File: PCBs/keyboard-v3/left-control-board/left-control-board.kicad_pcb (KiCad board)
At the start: 2 copper layers, 110.9 x 40 mm, 51 parts, among them J101 USB4510-03-1-A, J102 USB4510-03-1-A, J103 AMPHENOL_GSB12J21C1EU, J105 MSD-1-A, J501 Conn_02x08_Odd_Even, J601 F31Z1A7H111008, J602 F31Z1A7H111008, U101 USB2534-1080AEN, U102 STM32G0C1CEUx, U103 GL835, U104 USBLC6-4SC6, U201 USBLC6-4SC6, U701 TPS62290TDRVRQ1, Y101 CX2016SA24000D0HLLG3

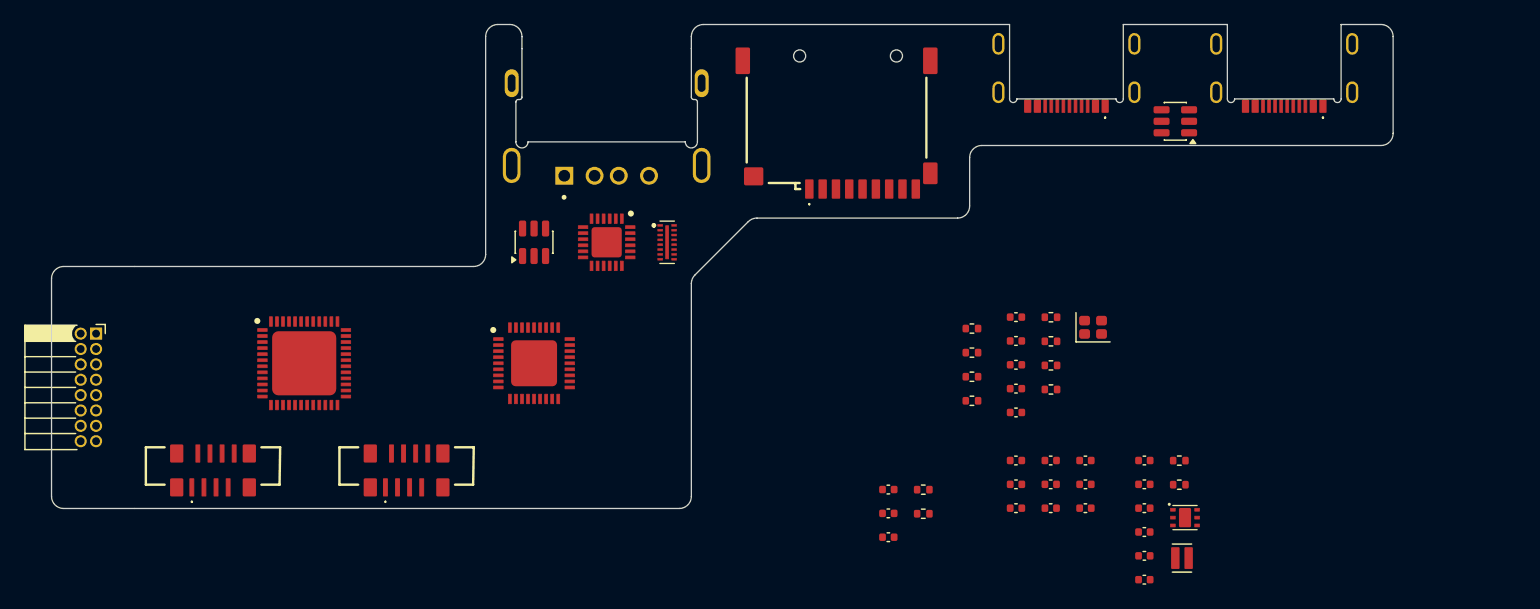
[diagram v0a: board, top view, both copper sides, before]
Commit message: Left knob board done
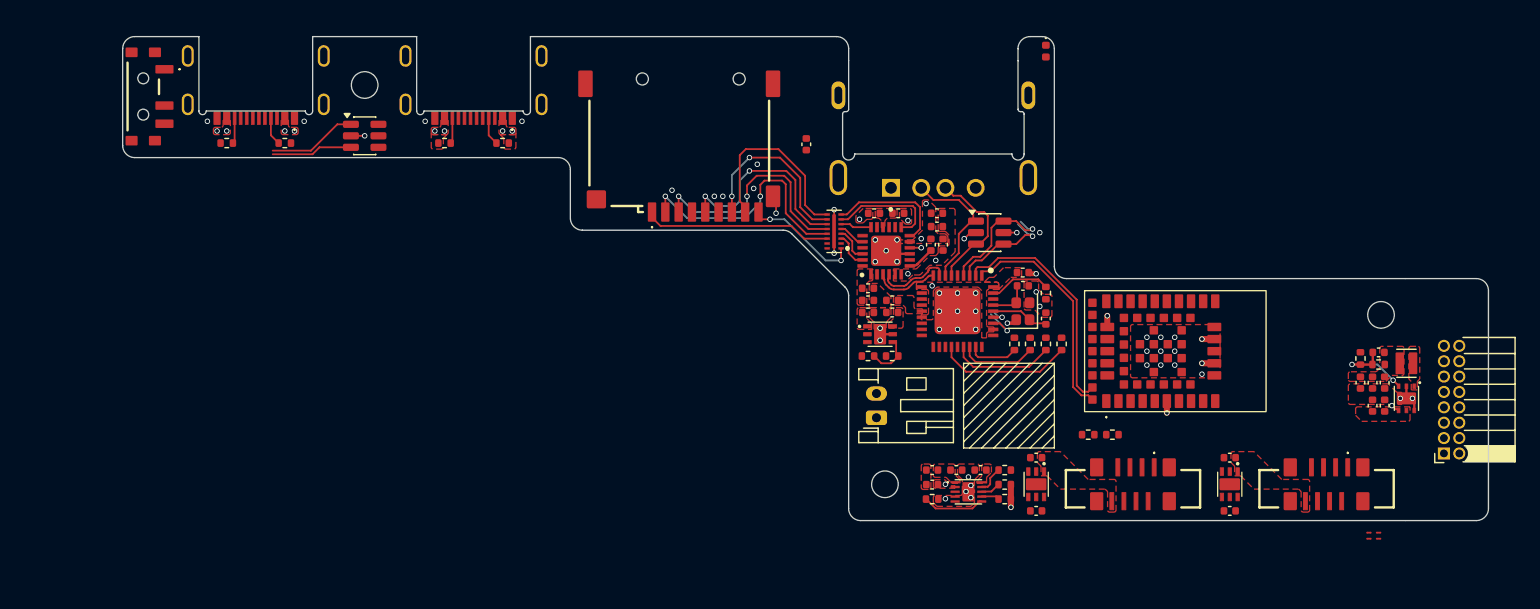
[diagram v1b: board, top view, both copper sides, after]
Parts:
- removed C109: 100n, project_footprints:C_0402
- removed C110: 1u, project_footprints:C_0402
- removed C111, C201, C202, C204, C205, C206: 4u7, project_footprints:C_0402
- removed C203: 22p, project_footprints:C_0402
- removed L201: 78438313015, project_footprints:L_Wurth_WE-MAIA-1610
- removed R101, R102: 10k, project_footprints:R_0402
- removed R203, R204: 5k1, project_footprints:R_0402
- removed U102: STM32G0C1CEUx, project_footprints:QFN50P700X700X60-49N-D
- added C601: 1u, project_footprints:C_0402, F.Cu at (175.5, 118.2)
- added C602: 1u, project_footprints:C_0402, F.Cu at (175.5, 113.8)
- added C603: 1u, project_footprints:C_0402, F.Cu at (191.5, 118.2)
- added C604: 1u, project_footprints:C_0402, F.Cu at (191.5, 113.8)
- added C701: 1u, project_footprints:C_0402, F.Cu at (170.9, 114.8)
- added C702: 4u7, project_footprints:C_0402, F.Cu at (168.9, 114.8)
- added C703: 4u7, project_footprints:C_0402, F.Cu at (166.9, 114.8)
- added C704: 1u, project_footprints:C_0402, F.Cu at (166.9, 116.0)
- added C705: 4u7, project_footprints:C_0402, F.Cu at (204.3, 109.5)
- added C706: 4u7, project_footprints:C_0402, F.Cu at (203.3, 109.5)
- added C707: 22p, project_footprints:C_0402, F.Cu at (203.8, 105.1)
- added C708: 4u7, project_footprints:C_0402, F.Cu at (204.3, 107.6)
- added C709: 4u7, project_footprints:C_0402, F.Cu at (203.3, 107.6)
- added C710: 4u7, project_footprints:C_0402, F.Cu at (202.3, 107.6)
- added C803: 1u, project_footprints:C_0402, F.Cu at (163.6, 101.8)
- added D701: RED, project_footprints:LED_0402, F.Cu at (176.3, 80.2)
- added H101: MountingHole, MountingHole:MountingHole_2.2mm_M2, F.Cu at (120.0, 83.0)
- added H102: MountingHole, MountingHole:MountingHole_2.2mm_M2, F.Cu at (163.0, 116.0)
- added H103: MountingHole, MountingHole:MountingHole_2.2mm_M2, F.Cu at (204.0, 102.0)
- added J701: Conn_01x02, Connector_JST:JST_PH_S2B-PH-K_1x02_P2.00mm_Horizontal, F.Cu at (162.3, 110.5)
- added L701: 78438313015, project_footprints:L_Wurth_WE-MAIA-1610, F.Cu at (206.1, 106.0)
- added NT601: NetTie_2, project_footprints:NetTie-2_SMD_Pad0.15mm, F.Cu at (203.0, 120.5)
- added NT602: NetTie_2, project_footprints:NetTie-2_SMD_Pad0.15mm, F.Cu at (203.0, 120.0)
- added NT603: NetTie_2, project_footprints:NetTie-2_SMD_Pad0.15mm, F.Cu at (203.8, 120.5)
- added NT604: NetTie_2, project_footprints:NetTie-2_SMD_Pad0.15mm, F.Cu at (203.8, 120.0)
- added R205: 5k1, project_footprints:R_0402, F.Cu at (108.6, 87.8)
- added R206: 5k1, project_footprints:R_0402, F.Cu at (113.4, 87.8)
- added R401: 806k, project_footprints:R_0402, F.Cu at (179.8, 111.9)
- added R402: 2M, project_footprints:R_0402, F.Cu at (181.8, 111.9)
- added R703: 13k, project_footprints:R_0402, F.Cu at (172.9, 117.2)
- added R704: 10k, project_footprints:R_0402, F.Cu at (166.9, 117.2)
- added R705: 806k, project_footprints:R_0402, F.Cu at (203.8, 106.1)
- added R706: 180k, project_footprints:R_0402, F.Cu at (202.3, 105.6)
- added R803: 10k, project_footprints:R_0402, F.Cu at (177.6, 104.4)
- added R804: 10k, project_footprints:R_0402, F.Cu at (176.3, 104.4)
- added R807: 10k, project_footprints:R_0402, F.Cu at (173.7, 104.4)
- added S701: PCM12SMTBR, project_footprints:PCM12SMTBR, F.Cu at (101.7, 84.0)
- added U401: NINA-B302-00B, project_footprints:NINAB30200B, F.Cu at (187.0, 105.0)
- added U601: NCP380HMU05AATBG, project_footprints:SON65P200X200X55-7N, F.Cu at (175.5, 116.0)
- added U602: NCP380HMU05AATBG, project_footprints:SON65P200X200X55-7N, F.Cu at (191.5, 116.0)
- added U702: TPS62290TDRVRQ1, project_footprints:SON65P200X200X80-7N, F.Cu at (206.1, 108.9)
- added U801: NCP380HMU05AATBG, project_footprints:SON65P200X200X55-7N, F.Cu at (162.6, 103.6)
- J204: renamed from J103; value AMPHENOL_GSB12J21C1EU -> GSB12J21C1EU
- R201, R202: value 5k1 -> 22k
- R701: value 820k -> 10k
- R702: value 182k -> 1k
- U701: value TPS62290TDRVRQ1 -> BQ25185DLHR; footprint project_footprints:SON65P200X200X80-7N -> project_footprints:SON40P220X200X80-11N
- moved J501 111.8 mm to (209.2, 113.5), turned to 180 degrees
- moved J602 92.0 mm to (199.5, 116.0), turned to 0 degrees
- moved J201 85.0 mm to (111.0, 79.0)
- moved J601 60.1 mm to (183.5, 116.0), turned to 0 degrees
- moved J202 49.0 mm to (129.0, 79.0)
- moved R202 46.9 mm to (126.6, 87.8)
- moved R201 41.7 mm to (131.4, 87.8), turned to 180 degrees
- moved C308 36.4 mm to (156.5, 87.9), turned to -90 degrees
- moved U802 35.3 mm to (169.0, 101.7), turned to -90 degrees
- moved J204 27.0 mm to (167.0, 81.0)
- moved C302 25.3 mm to (162.1, 93.6), turned to 180 degrees
- moved C309 25.2 mm to (166.8, 96.2), turned to 90 degrees
- moved C305 24.3 mm to (167.3, 93.6), turned to 180 degrees
- moved C306 23.5 mm to (167.8, 96.2), turned to 90 degrees
- moved U103 23.1 mm to (163.1, 96.7), turned to 90 degrees
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- renumbered C105 to C801, C106 to C802, C101 to C804, C102 to C805, C103 to C806, J101 to J201, J102 to J202, R105 to R801, R104 to R802, R103 to R805, R108 to R806, U104 to U201, U201 to U202, U101 to U802, Y101 to Y801
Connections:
- C305 pad 1: +3V3 -> +3V3_USB
- C306 pad 1: +3V3 -> +3V3_USB
- C307 pad 1: +3V3 -> +3V3_USB
- C801 pad 1: +3V3 -> +3V3_USB
- C802 pad 1: +3V3 -> +3V3_USB
- J204 pad 2: /USB Connectors/USB2.DP -> /USB Connectors/USB3.DP
- J204 pad 3: /USB Connectors/USB2.DN -> /USB Connectors/USB3.DN
- J501 pad 1: unconnected-(J501-Pin_1-Pad1) -> /Debug Connector/CTRL.SWDIO
- J501 pad 10: unconnected-(J501-Pin_10-Pad10) -> /Daughter Board Connectors/KEYS.SWCLK
- J501 pad 11: unconnected-(J501-Pin_11-Pad11) -> GND
- J501 pad 12: unconnected-(J501-Pin_12-Pad12) -> /Daughter Board Connectors/KEYS.RX
- J501 pad 13: unconnected-(J501-Pin_13-Pad13) -> /Daughter Board Connectors/~{KEYS_RST}
- J501 pad 14: unconnected-(J501-Pin_14-Pad14) -> GND
- J501 pad 15: unconnected-(J501-Pin_15-Pad15) -> +3V3
- J501 pad 16: unconnected-(J501-Pin_16-Pad16) -> +VSYS
- J501 pad 2: unconnected-(J501-Pin_2-Pad2) -> /Debug Connector/CTRL.SWCLK
- J501 pad 3: unconnected-(J501-Pin_3-Pad3) -> GND
- J501 pad 4: unconnected-(J501-Pin_4-Pad4) -> GND
- J501 pad 5: unconnected-(J501-Pin_5-Pad5) -> /Daughter Board Connectors/KNOB.SWDIO
- J501 pad 6: unconnected-(J501-Pin_6-Pad6) -> /Daughter Board Connectors/KNOB.SWCLK
- J501 pad 7: unconnected-(J501-Pin_7-Pad7) -> GND
- J501 pad 8: unconnected-(J501-Pin_8-Pad8) -> /Daughter Board Connectors/KNOB.RX
- J501 pad 9: unconnected-(J501-Pin_9-Pad9) -> /Daughter Board Connectors/KEYS.SWDIO
- J601 pad 2: /Daughter Board Connectors/KNOB.SWDIO -> /Daughter Board Connectors/KNOB_SWDIO/~{KNOB_INT}
- J601 pad 8: VBUS -> /Daughter Board Connectors/KNOB_5V
- J602 pad 2: /Daughter Board Connectors/KEYS.SWDIO -> /Daughter Board Connectors/KEYS_SWDIO/~{INT}
- J602 pad 8: VBUS -> /Daughter Board Connectors/KEYS_5V
- R201 pad 1: /USB Connectors/USB1_CC2 -> VBUS
- R201 pad 2: GND -> /USB Connectors/USB1_CC1
- R202 pad 1: /USB Connectors/USB1_CC1 -> VBUS
- R202 pad 2: GND -> /USB Connectors/USB1_CC2
- R701 pad 1: +3V3 -> VBUS
- R701 pad 2: /Power/FB_1V8 -> /Power/STAT1
- R702 pad 1: /Power/FB_1V8 -> /Power/ISET
- R806 pad 1: /USB Hub/CFG_SEL1 -> GND
- R806 pad 2: GND -> /USB Hub/CFG_SEL1
- U103 pad 5: +3V3 -> +3V3_USB
- U103 pad 6: +3V3 -> +3V3_USB
- U201 pad 1: /USB Connectors/USB0.DP -> /USB Connectors/USB3.DP
- U201 pad 3: /USB Connectors/USB0.DN -> /USB Connectors/USB3.DN
- U201 pad 4: unconnected-(U104-I/O3-Pad4) -> /USB Connectors/USB1.DN
- U201 pad 6: unconnected-(U104-I/O4-Pad6) -> /USB Connectors/USB1.DP
- U202 pad 1: /USB Connectors/USB1.DP -> /USB Connectors/USB0.DP
- U202 pad 3: /USB Connectors/USB1.DN -> /USB Connectors/USB0.DN
- U202 pad 4: /USB Connectors/USB2.DP -> unconnected-(U202-I/O3-Pad4)
- U202 pad 6: /USB Connectors/USB2.DN -> unconnected-(U202-I/O4-Pad6)
- U701 pad 1: /Power/SW_1V8 -> +VSYS
- U701 pad 2: VBUS -> /Power/BAT
- U701 pad 3: /Power/FB_1V8 -> /Power/STAT2
- U701 pad 4: VBUS -> GND
- U701 pad 5: VBUS -> GND
- U701 pad 6: GND -> /Power/TS
- U701 pad 7: GND -> /Power/ILIM/VSET
- U802 pad 1: /USB Connectors/USB1.DN -> /MCU/DN
- U802 pad 10: +3V3 -> +3V3_USB
- U802 pad 15: +3V3 -> +3V3_USB
- U802 pad 2: /USB Connectors/USB1.DP -> /MCU/DP
- U802 pad 23: +3V3 -> +3V3_USB
- U802 pad 26: /Daughter Board Connectors/~{KEYS_RST} -> /USB Hub/~{RST}
- U802 pad 29: +3V3 -> +3V3_USB
- U802 pad 3: /USB Connectors/USB2.DN -> /USB Connectors/USB1.DN
- U802 pad 36: +3V3 -> +3V3_USB
- U802 pad 4: /USB Connectors/USB2.DP -> /USB Connectors/USB1.DP
- U802 pad 6: /SD Card/DN -> /USB Connectors/USB3.DN
- U802 pad 7: /SD Card/DP -> /USB Connectors/USB3.DP
- U802 pad 8: /MCU/DN -> /SD Card/DN
- U802 pad 9: /MCU/DP -> /SD Card/DP
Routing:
- net /SD Card/SD_D3_EX: track 0.00 -> 20.7 mm, vias 0 -> 2
- net /MCU/DP: track 0.00 -> 19.5 mm
- net /SD Card/SD_CMD_EX: track 0.00 -> 19.4 mm, vias 0 -> 2
- net GND: track 0.00 -> 19.1 mm, vias 0 -> 61
- net /MCU/DN: track 0.00 -> 18.4 mm
- net /SD Card/SD_CLK_EX: track 0.00 -> 17.1 mm, vias 0 -> 2
- net /SD Card/SD_D1_EX: track 0.00 -> 16.0 mm
- net /SD Card/SD_D2_EX: track 0.00 -> 15.6 mm
- net /SD Card/SD_D0_EX: track 0.00 -> 15.1 mm, vias 0 -> 2
- net /MCU/SDA: track 0.00 -> 11.2 mm
- net /USB Connectors/USB3.DP: track 0.00 -> 11.2 mm
- net /USB Connectors/USB3.DN: track 0.00 -> 10.9 mm
- net /USB Connectors/USB1.DP: track 0.00 -> 10.5 mm, vias 0 -> 1
- net /SD Card/CD: track 0.00 -> 10.2 mm, vias 0 -> 3
- net /USB Connectors/USB0.DN: track 0.00 -> 10.0 mm, vias 0 -> 1
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- added copper zone on F.Cu, net +1V2
- added copper zone on F.Cu, net +3V3
- added copper zone on F.Cu, net +3V3_USB
- added copper zone on F.Cu, net +VSYS
- added copper zone on F.Cu, net /Daughter Board Connectors/KEYS_5V
- added copper zone on F.Cu, net /Daughter Board Connectors/KNOB_5V
- added copper zone on F.Cu, net /Power/BAT
- added copper zone on F.Cu, net /Power/SW_3V3
- added copper zone on F.Cu, net /SD Card/SDREG
- added copper zone on F.Cu, net /SD Card/VDD
- added copper zone on F.Cu, net GND
- added copper zone on In1.Cu, net GND
- added copper zone on In2.Cu, net GND
- added copper zone on F.Cu, net VBUS
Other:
- board size 110.9 x 40 mm -> 112.9 x 40 mm
- copper layers 2 -> 4

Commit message: Left control board done
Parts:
- NT601, NT603: moved to B.Cu
- moved NT602 22.9 mm to (182.3, 110.2), turned to -90 degrees
- moved R402 12.0 mm to (179.0, 100.2), turned to 90 degrees
- moved NT604 10.8 mm to (196.0, 112.5)
- moved NT601 9.99 mm to (193.3, 117.9)
- moved R401 9.73 mm to (179.0, 102.2), turned to 90 degrees
- moved NT603 6.26 mm to (201.0, 114.9)
- moved U401 1.00 mm to (188.0, 105.0)
- turned J601 to 180 degrees
- turned J602 to 180 degrees
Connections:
- U401 pad 1: unconnected-(U401-P0.13-Pad1) -> /Daughter Board Connectors/~{KNOB_INT}
- U401 pad 2: unconnected-(U401-P0.14-Pad2) -> /Daughter Board Connectors/KNOB.TX
- U401 pad 25: unconnected-(U401-P0.04-Pad25) -> /MCU/VSENSE
- U401 pad 3: unconnected-(U401-P0.15-Pad3) -> /Daughter Board Connectors/KNOB.RX
- U401 pad 4: unconnected-(U401-P0.16-Pad4) -> /Daughter Board Connectors/KEYS_5V_EN
- U401 pad 5: unconnected-(U401-P0.24-Pad5) -> /Daughter Board Connectors/~{KEYS_INT}
- U401 pad 50: unconnected-(U401-P0.20/QSPI_D0-Pad50) -> /MCU/SCL
- U401 pad 51: unconnected-(U401-P0.17/QSPI_CS-Pad51) -> /MCU/SDA
- U401 pad 52: unconnected-(U401-P0.19/QSPI_CLK-Pad52) -> /Daughter Board Connectors/KNOB_5V_EN
- U401 pad 7: unconnected-(U401-P0.25-Pad7) -> /Daughter Board Connectors/KEYS.TX
- U401 pad 8: unconnected-(U401-P1.00/SWO/TRACE_D0-Pad8) -> /Daughter Board Connectors/KEYS.RX
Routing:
- net /Power/EN: track 0.72 -> 143.5 mm, vias 1 -> 6
- net +VSYS: track 0.00 -> 133.8 mm, vias 0 -> 18
- net /Daughter Board Connectors/~{KEYS_RST}: track 0.00 -> 71.0 mm, vias 0 -> 6
- net /USB Connectors/USB0.DP: track 8.88 -> 78.2 mm, vias 1 -> 4
- net /USB Connectors/USB0.DN: track 10.0 -> 77.8 mm, vias 1 -> 4
- net /USB Connectors/USB1.DN: track 8.69 -> 64.3 mm, vias 1 -> 4
- net /USB Connectors/USB1.DP: track 10.5 -> 62.2 mm, vias 1 -> 4
- net /Power/STAT2: track 0.00 -> 50.0 mm, vias 0 -> 2
- net /Daughter Board Connectors/KNOB.RX: track 0.00 -> 42.7 mm, vias 0 -> 2
- net /Daughter Board Connectors/KEYS.RX: track 0.00 -> 40.8 mm, vias 0 -> 2
- net +3V3: track 0.00 -> 40.2 mm, vias 0 -> 12
- net /Power/STAT1: track 2.27 -> 39.1 mm, vias 0 -> 2
- net /Daughter Board Connectors/KNOB.SWCLK: track 0.00 -> 35.9 mm, vias 0 -> 2
- net GND: track 19.1 -> 50.2 mm, vias 61 -> 120
- net /Debug Connector/CTRL.SWDIO: track 0.00 -> 25.5 mm
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- added copper zone on B.Cu, net +3V3
- added copper zone on B.Cu, net +3V3_USB
- added copper zone on B.Cu, net +VSYS
- added copper zone on B.Cu, net /Daughter Board Connectors/KEYS_5V
- added copper zone on B.Cu, net /Daughter Board Connectors/KNOB_5V
- added copper zone on B.Cu, net /Power/BAT
- added copper zone on B.Cu, net /SD Card/SD_VCC
- added copper zone on F.Cu, net /SD Card/SD_VCC
- added copper zone on B.Cu, net VBUS

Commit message: Keyboard v3 hardware done
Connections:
- net /USB Connectors/USB1.DN renamed /USB Connectors/USB2.DN
- net /USB Connectors/USB1.DP renamed /USB Connectors/USB2.DP
- net /USB Connectors/USB1_CC1 renamed /USB Connectors/USB2_CC1
- net /USB Connectors/USB1_CC2 renamed /USB Connectors/USB2_CC2
- S701 pad 1: +VSYS -> GND
- S701 pad 3: GND -> +VSYS
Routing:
- net +VSYS: track 133.8 -> 128.9 mm
- net GND: track 50.2 -> 51.8 mm
- net /Daughter Board Connectors/~{KEYS_RST}: track 71.0 -> 70.4 mm
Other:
- board text added: "+"
- board text added: "-"
- board text added: "Keyboard v3 Left Control Board Ben Smith 2026"
- board text added: "Off"
- board text added: "On"

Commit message: Added v3 left BOMs and updated buck inductor
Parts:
- L701: value 78438313015 -> 74438313015; footprint project_footprints:L_Wurth_WE-MAIA-1610 -> project_footprints:L_Wurth_WE-MAPI-1610
